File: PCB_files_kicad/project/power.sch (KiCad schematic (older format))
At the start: 21 parts, among them J7 Barrel_Jack, J8 USB_B_Micro, Q1 IRF7240PBF, U2 TP4056, U3 MT3608

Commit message: PCB - Placing components
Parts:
- BT1: footprint (none) -> TerminalBlock:TerminalBlock_bornier-2_P5.08mm
- C1, C2, C3, C5: footprint (none) -> Capacitor_THT:C_Disc_D5.0mm_W2.5mm_P5.00mm
- D3: footprint (none) -> Diode_THT:D_DO-15_P12.70mm_Horizontal
- D4: footprint (none) -> LED_THT:LED_D5.0mm; Mouser Link https://ar.mouser.com/ProductDetail/Wurth-Elektronik/150060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 -> (none); Mouser Number 710-150060VS75000 -> (none); Part Number 150060VS75000 -> (none)
- D5: value CDBU0130L - 350mV -> SS34; footprint (none) -> Diode_THT:D_DO-15_P12.70mm_Horizontal; Mouser Link https://ar.mouser.com/ProductDetail/Comchip-Technology/CDBU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 -> (none); Mouser Number 750-CDBU0130L -> (none); Part Number CDBU0130L -> (none)
- J7: footprint (none) -> Connector_BarrelJack:BarrelJack_Horizontal
- J8: footprint (none) -> Connector_USB:USB_Micro-B_Amphenol_10104110_Horizontal
- L1: footprint (none) -> Inductor_THT:L_Radial_D6.0mm_P4.00mm
- R10: value 15k -> 16k-THT; footprint (none) -> Resistor_THT:R_Axial_DIN0414_L11.9mm_D4.5mm_P20.32mm_Horizontal; Mouser Link https://ar.mouser.com/ProductDetail/Bourns/CR0603-FX-1403EL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 -> (none); Mouser Number 652-CR0603FX-1403ELF -> (none); Part Number CR0603-FX-1403ELF -> (none)
- R11: value 2k -> 2k2; footprint (none) -> Resistor_THT:R_Axial_DIN0414_L11.9mm_D4.5mm_P20.32mm_Horizontal; Mouser Link https://ar.mouser.com/ProductDetail/Bourns/CR0603-FX-1403EL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 -> (none); Mouser Number 652-CR0603FX-1403ELF -> (none); Part Number CR0603-FX-1403ELF -> (none)
- R3, R4: footprint (none) -> Resistor_THT:R_Axial_DIN0414_L11.9mm_D4.5mm_P20.32mm_Horizontal
- R7: footprint (none) -> Resistor_THT:R_Axial_DIN0414_L11.9mm_D4.5mm_P20.32mm_Horizontal; Mouser Link https://ar.mouser.com/ProductDetail/Bourns/CR0603-FX-1403EL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 -> (none); Mouser Number 652-CR0603FX-1403ELF -> (none); Part Number CR0603-FX-1403ELF -> (none)
- U2: footprint (none) -> Package_TO_SOT_SMD:SC-70-8_Handsoldering
- U3: footprint Package_TO_SOT_SMD:SOT-23-6 -> Package_TO_SOT_SMD:SOT-23-6_Handsoldering

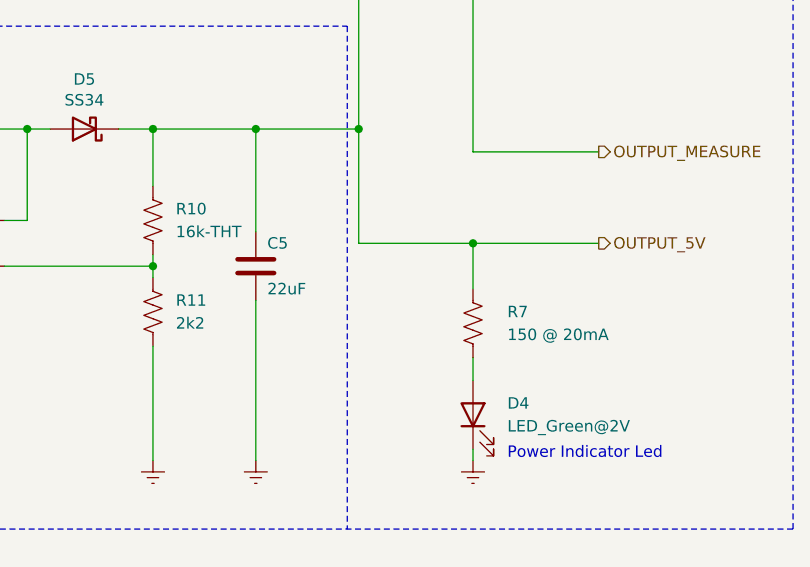
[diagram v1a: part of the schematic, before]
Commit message: PCB - Starting to route
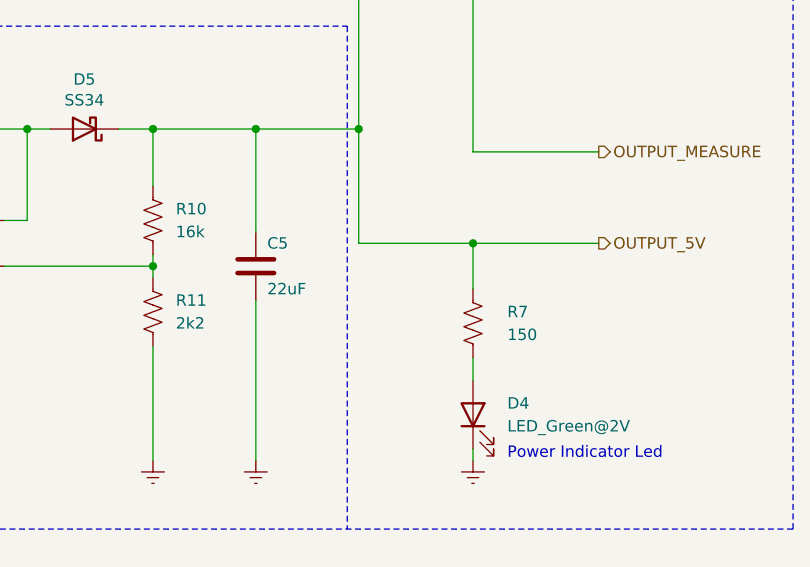
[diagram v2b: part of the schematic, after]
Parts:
- BT1: footprint TerminalBlock:TerminalBlock_bornier-2_P5.08mm -> mylib:Batt
- R10: value 16k-THT -> 16k
- R7: value 150 @ 20mA -> 150
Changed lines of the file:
@@
 F 0 "BT1" H 4350 3800 50  0000 L CNN
 F 1 "Batt" H 4350 3600 50  0000 L CNN
-F 2 "TerminalBlock:TerminalBlock_bornier-2_P5.08mm" V 4550 3710 50  0001 C CNN
+F 2 "mylib:Batt" V 4550 3710 50  0001 C CNN
 F 3 "http://www.batteryspace.com/prod-specs/4869.pdf" V 4550 3710 50  0001 C CNN
 F 4 "https://articulo.mercadolibre.com.ar/MLA-903149783-celda-18650-lg-2200mah-con-terminal-para-soldar-37v-42v-_JM?matt_tool=88481412&matt_word=&matt_source=google&matt_campaign_id=11618987428&matt_ad_group_id=113657532672&matt_match_type=&matt_network=g&matt_device=m&matt_creative=479785004862&matt_keyword=&matt_ad_position=&matt_ad_type=pla&matt_merchant_id=334313049&matt_product_id=MLA903149783&matt_product_partition_id=758317414930&matt_target_id=aud-415044759576:pla-758317414930&gclid=EAIaIQobChMI6N6ysO338QIVsyCtBh2hBgntEAQYASABEgKf_vD_BwE" H 4550 3650 50  0001 C CNN "Mouser Link"
@@
 AR Path="/60FFCFF1/6124D4A7" Ref="R7"  Part="1"
 F 0 "R7" H 9550 4100 50  0000 L CNN
-F 1 "150 @ 20mA" H 9550 4000 50  0000 L CNN
+F 1 "150" H 9550 4000 50  0000 L CNN
 F 2 "Resistor_THT:R_Axial_DIN0414_L11.9mm_D4.5mm_P20.32mm_Horizontal" V 9440 4040 50  0001 C CNN
 F 3 "" H 9400 4050 50  0001 C CNN
@@
 AR Path="/60FFCFF1/61443227" Ref="R10"  Part="1"
 F 0 "R10" H 8100 3650 50  0000 L CNN
-F 1 "16k-THT" H 8100 3550 50  0000 L CNN
+F 1 "16k" H 8100 3550 50  0000 L CNN
 F 2 "Resistor_THT:R_Axial_DIN0414_L11.9mm_D4.5mm_P20.32mm_Horizontal" V 8040 3590 50  0001 C CNN
 F 3 "" H 8000 3600 50  0001 C CNN

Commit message: SCH version 1.3
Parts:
- added TP1: PowerSupply, TestPoint:TestPoint_THTPad_D2.0mm_Drill1.0mm, symbol Connector:TestPoint
- added TP2: Batt, TestPoint:TestPoint_THTPad_D2.0mm_Drill1.0mm, symbol Connector:TestPoint
- added TP3: Qdrain, TestPoint:TestPoint_THTPad_D2.0mm_Drill1.0mm, symbol Connector:TestPoint
- added TP4: out5v, TestPoint:TestPoint_THTPad_D2.0mm_Drill1.0mm, symbol Connector:TestPoint
- Q1: value IRF7240PBF -> Irf9z20; footprint Package_TO_SOT_SMD:TO-252-2 -> Package_TO_SOT_THT:TO-220-3_Vertical
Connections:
- net OUTPUT_5V: now also TP4.1
- net OUTPUT_BAT: now also TP2.1
- net OUTPUT_MEASURE: now also TP1.1
- net at C3.1, L1.1, Q1.2 (D)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: now also TP3.1
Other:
- note added: "|VGS(ON)| > |-3.7v|"
- note removed: "-4.5v > VGS"
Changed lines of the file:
@@
 Sheet 2 3
 Title "Sistema de Alarma"
-Date "2021-07-23"
-Rev "v1.2"
+Date "2021-09-15"
+Rev "v1.3"
 Comp "Proyecto Técnicas Digitales II - Grupo N°4"
 Comment1 "Liaño, Lucas"
@@
 P 5650 3100
 F 0 "Q1" V 5550 2950 50  0000 C CNN
-F 1 "IRF7240PBF" V 5600 3450 50  0000 C CNN
-F 2 "Package_TO_SOT_SMD:TO-252-2" H 5850 3200 50  0001 C CNN
-F 3 "https://pdf1.alldatasheet.es/datasheet-pdf/view/68328/IRF/IRF9540N.html" H 5650 3100 50  0001 C CNN
+F 1 "Irf9z20" V 5550 3300 50  0000 C CNN
+F 2 "Package_TO_SOT_THT:TO-220-3_Vertical" H 5850 3200 50  0001 C CNN
+F 3 "https://www.vishay.com/docs/90121/sihf9z20.pdf" H 5650 3100 50  0001 C CNN
 F 4 "" H 5650 3100 50  0001 C CNN "Mouser Link"
 F 5 "ver en electrocomponentes!" H 5650 3100 50  0001 C CNN "Mouser Number"
@@
 	1    0    0    -1
 $EndComp
-Text Notes 5350 3500 0    50   ~ 0
--4.5v > VGS
+Text Notes 5400 3500 0    30   ~ 0
+|VGS(ON)| > |-3.7v|
 $Comp
 L Device:R_US R?
@@
 EndData
 $EndBitmap
+$Comp
+L Connector:TestPoint TP1
+U 1 1 6136A15D
+P 3450 2450
+F 0 "TP1" H 3508 2568 50  0000 L CNN
+F 1 "PowerSupply" H 3500 2650 50  0000 L CNN
+F 2 "TestPoint:TestPoint_THTPad_D2.0mm_Drill1.0mm" H 3650 2450 50  0001 C CNN
+F 3 "~" H 3650 2450 50  0001 C CNN
+	1    3450 2450
+	1    0    0    -1
+$EndComp
+$Comp
+L Connector:TestPoint TP2
+U 1 1 6136C229
+P 5100 3200
+F 0 "TP2" H 5158 3318 50  0000 L CNN
+F 1 "Batt" H 5150 3250 50  0000 L CNN
+F 2 "TestPoint:TestPoint_THTPad_D2.0mm_Drill1.0mm" H 5300 3200 50  0001 C CNN
+F 3 "~" H 5300 3200 50  0001 C CNN
+	1    5100 3200
+	1    0    0    -1
+$EndComp
+$Comp
+L Connector:TestPoint TP3
+U 1 1 613711A3
+P 6050 3200
+F 0 "TP3" H 6108 3318 50  0000 L CNN
+F 1 "Qdrain" H 6100 3250 50  0000 L CNN
+F 2 "TestPoint:TestPoint_THTPad_D2.0mm_Drill1.0mm" H 6250 3200 50  0001 C CNN
+F 3 "~" H 6250 3200 50  0001 C CNN
+	1    6050 3200
+	1    0    0    -1
+$EndComp
+$Comp
+L Connector:TestPoint TP4
+U 1 1 61377A4F
+P 9400 3700
+F 0 "TP4" H 9458 3818 50  0000 L CNN
+F 1 "out5v" H 9450 3750 50  0000 L CNN
+F 2 "TestPoint:TestPoint_THTPad_D2.0mm_Drill1.0mm" H 9600 3700 50  0001 C CNN
+F 3 "~" H 9600 3700 50  0001 C CNN
+	1    9400 3700
+	1    0    0    -1
+$EndComp
 $EndSCHEMATC

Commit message: Lot of changes.. BOM was added and UTN logo too
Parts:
- C3: value 22uF-X5R -> 22uF
- Q1: value Irf9z20 -> IRF9Z20
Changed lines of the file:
@@
 P 5650 3100
 F 0 "Q1" V 5550 2950 50  0000 C CNN
-F 1 "Irf9z20" V 5550 3300 50  0000 C CNN
+F 1 "IRF9Z20" V 5550 3300 50  0000 C CNN
 F 2 "Package_TO_SOT_THT:TO-220-3_Vertical" H 5850 3200 50  0001 C CNN
 F 3 "https://www.vishay.com/docs/90121/sihf9z20.pdf" H 5650 3100 50  0001 C CNN
@@
 AR Path="/60FFCFF1/61045CAF" Ref="C3"  Part="1"
 F 0 "C3" H 6100 4000 50  0000 L CNN
-F 1 "22uF-X5R" H 6100 3800 50  0000 L CNN
+F 1 "22uF" H 6100 3800 50  0000 L CNN
 F 2 "Capacitor_THT:C_Disc_D5.0mm_W2.5mm_P5.00mm" H 6088 3750 50  0001 C CNN
 F 3 "~" H 6050 3900 50  0001 C CNN
@@
 Text HLabel 9950 3700 2    50   Output ~ 0
 OUTPUT_5V
-Text Notes 1200 7650 0    50   ~ 10
-Circuit reference: https://www.youtube.com/watch?v=GRd9uTwg7r4
 Wire Wire Line
 	4850 2450 4850 2100
@@
 	1    0    0    -1
 $EndComp
+Text Notes 1200 7650 0    50   ~ 10
+Circuit reference: https://www.youtube.com/watch?v=GRd9uTwg7r4
 $EndSCHEMATC

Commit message: Sche rev 1.4 - PCB rev 1.2
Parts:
- C1, C2, C3, C5: footprint Capacitor_THT:C_Disc_D5.0mm_W2.5mm_P5.00mm -> Capacitor_THT:CP_Radial_D5.0mm_P2.50mm
- R10, R11, R3, R4, R7: footprint Resistor_THT:R_Axial_DIN0414_L11.9mm_D4.5mm_P20.32mm_Horizontal -> Resistor_THT:R_Axial_DIN0309_L9.0mm_D3.2mm_P12.70mm_Horizontal
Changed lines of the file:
@@
 Sheet 2 3
 Title "Sistema de Alarma"
-Date "2021-09-15"
-Rev "v1.3"
+Date "2021-09-23"
+Rev "v1.4"
 Comp "Proyecto Técnicas Digitales II - Grupo N°4"
 Comment1 "Liaño, Lucas"
@@
 F 0 "C1" H 2450 3850 50  0000 L CNN
 F 1 "10uF" H 2400 3650 50  0000 L CNN
-F 2 "Capacitor_THT:C_Disc_D5.0mm_W2.5mm_P5.00mm" H 2638 3600 50  0001 C CNN
+F 2 "Capacitor_THT:CP_Radial_D5.0mm_P2.50mm" H 2638 3600 50  0001 C CNN
 F 3 "~" H 2600 3750 50  0001 C CNN
 	1    2600 3750
@@
 F 0 "R4" H 4918 2796 50  0000 L CNN
 F 1 "10k" H 4918 2705 50  0000 L CNN
-F 2 "Resistor_THT:R_Axial_DIN0414_L11.9mm_D4.5mm_P20.32mm_Horizontal" V 4890 2740 50  0001 C CNN
+F 2 "Resistor_THT:R_Axial_DIN0309_L9.0mm_D3.2mm_P12.70mm_Horizontal" V 4890 2740 50  0001 C CNN
 F 3 "~" H 4850 2750 50  0001 C CNN
 	1    4850 2750
@@
 F 0 "C5" H 8500 3900 50  0000 L CNN
 F 1 "22uF" H 8500 3700 50  0000 L CNN
-F 2 "Capacitor_THT:C_Disc_D5.0mm_W2.5mm_P5.00mm" H 8488 3650 50  0001 C CNN
+F 2 "Capacitor_THT:CP_Radial_D5.0mm_P2.50mm" H 8488 3650 50  0001 C CNN
 F 3 "~" H 8450 3800 50  0001 C CNN
 	1    8450 3800
@@
 F 0 "C3" H 6100 4000 50  0000 L CNN
 F 1 "22uF" H 6100 3800 50  0000 L CNN
-F 2 "Capacitor_THT:C_Disc_D5.0mm_W2.5mm_P5.00mm" H 6088 3750 50  0001 C CNN
+F 2 "Capacitor_THT:CP_Radial_D5.0mm_P2.50mm" H 6088 3750 50  0001 C CNN
 F 3 "~" H 6050 3900 50  0001 C CNN
 	1    6050 3900
@@
 F 0 "R3" H 4218 4146 50  0000 L CNN
 F 1 "2.4k" H 4218 4055 50  0000 L CNN
-F 2 "Resistor_THT:R_Axial_DIN0414_L11.9mm_D4.5mm_P20.32mm_Horizontal" V 4190 4090 50  0001 C CNN
+F 2 "Resistor_THT:R_Axial_DIN0309_L9.0mm_D3.2mm_P12.70mm_Horizontal" V 4190 4090 50  0001 C CNN
 F 3 "~" H 4150 4100 50  0001 C CNN
 	1    4150 4100
@@
 F 0 "R7" H 9550 4100 50  0000 L CNN
 F 1 "150" H 9550 4000 50  0000 L CNN
-F 2 "Resistor_THT:R_Axial_DIN0414_L11.9mm_D4.5mm_P20.32mm_Horizontal" V 9440 4040 50  0001 C CNN
+F 2 "Resistor_THT:R_Axial_DIN0309_L9.0mm_D3.2mm_P12.70mm_Horizontal" V 9440 4040 50  0001 C CNN
 F 3 "" H 9400 4050 50  0001 C CNN
 F 4 "" H 9400 4050 50  0001 C CNN "Mouser Link"
@@
 F 0 "C2" H 4950 3700 50  0000 L CNN
 F 1 "10uF" H 4900 3450 50  0000 L CNN
-F 2 "Capacitor_THT:C_Disc_D5.0mm_W2.5mm_P5.00mm" H 5138 3450 50  0001 C CNN
+F 2 "Capacitor_THT:CP_Radial_D5.0mm_P2.50mm" H 5138 3450 50  0001 C CNN
 F 3 "~" H 5100 3600 50  0001 C CNN
 	1    5100 3600
@@
 F 0 "R10" H 8100 3650 50  0000 L CNN
 F 1 "16k" H 8100 3550 50  0000 L CNN
-F 2 "Resistor_THT:R_Axial_DIN0414_L11.9mm_D4.5mm_P20.32mm_Horizontal" V 8040 3590 50  0001 C CNN
+F 2 "Resistor_THT:R_Axial_DIN0309_L9.0mm_D3.2mm_P12.70mm_Horizontal" V 8040 3590 50  0001 C CNN
 F 3 "" H 8000 3600 50  0001 C CNN
 F 4 "" H 8000 3600 50  0001 C CNN "Mouser Link"
@@
 F 0 "R11" H 8100 4050 50  0000 L CNN
 F 1 "2k2" H 8100 3950 50  0000 L CNN
-F 2 "Resistor_THT:R_Axial_DIN0414_L11.9mm_D4.5mm_P20.32mm_Horizontal" V 8040 3990 50  0001 C CNN
+F 2 "Resistor_THT:R_Axial_DIN0309_L9.0mm_D3.2mm_P12.70mm_Horizontal" V 8040 3990 50  0001 C CNN
 F 3 "" H 8000 4000 50  0001 C CNN
 F 4 "" H 8000 4000 50  0001 C CNN "Mouser Link"

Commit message: Schematic v1.5 - PCB v1.3
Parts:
- D3: value CDBU0130L - 350mV -> 1N5822 - 500mV; footprint Diode_THT:D_DO-15_P12.70mm_Horizontal -> Diode_THT:D_DO-201AD_P15.24mm_Horizontal; Mouser Link https://ar.mouser.com/ProductDetail/Comchip-Technology/CDBU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 -> (none); Mouser Number 750-CDBU0130L -> (none); Part Number CDBU0130L -> (none)
- D5: value SS34 -> 1N5822 - 500mV; footprint Diode_THT:D_DO-15_P12.70mm_Horizontal -> Diode_THT:D_DO-201AD_P15.24mm_Horizontal
- R10: value 16k -> 15k
- R3: value 2.4k -> 2k2
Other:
- note added: "Battery Charge Module @ 545mA\n\n"
- note removed: "Battery Charge Module @ 500mA\n\n"
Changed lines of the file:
@@
 Sheet 2 3
 Title "Sistema de Alarma"
-Date "2021-09-23"
-Rev "v1.4"
+Date "2021-09-26"
+Rev "v1.5"
 Comp "Proyecto Técnicas Digitales II - Grupo N°4"
 Comment1 "Liaño, Lucas"
@@
 P 6150 2450
 F 0 "D3" H 6150 2233 50  0000 C CNN
-F 1 "CDBU0130L - 350mV" H 6150 2324 50  0000 C CNN
-F 2 "Diode_THT:D_DO-15_P12.70mm_Horizontal" H 6150 2450 50  0001 C CNN
-F 3 "https://ar.mouser.com/datasheet/2/80/CDBU0130L_HF_RevA748574-2490037.pdf" H 6150 2450 50  0001 C CNN
-F 4 "https://ar.mouser.com/ProductDetail/Comchip-Technology/CDBU0130L?qs=tw%252BuQ%2FB6PO2Mup5%252Bk7mubQ%3D%3D" H 6150 2450 50  0001 C CNN "Mouser Link"
-F 5 "750-CDBU0130L " H 6150 2450 50  0001 C CNN "Mouser Number"
-F 6 "CDBU0130L " H 6150 2450 50  0001 C CNN "Part Number"
+F 1 "1N5822 - 500mV" H 6150 2324 50  0000 C CNN
+F 2 "Diode_THT:D_DO-201AD_P15.24mm_Horizontal" H 6150 2450 50  0001 C CNN
+F 3 "https://www.vishay.com/docs/88526/1n5820.pdf" H 6150 2450 50  0001 C CNN
+F 4 "" H 6150 2450 50  0001 C CNN "Mouser Link"
+F 5 "" H 6150 2450 50  0001 C CNN "Mouser Number"
+F 6 "" H 6150 2450 50  0001 C CNN "Part Number"
 	1    6150 2450
 	-1   0    0    1
@@
 AR Path="/60FFCFF1/61001D30" Ref="R3"  Part="1"
 F 0 "R3" H 4218 4146 50  0000 L CNN
-F 1 "2.4k" H 4218 4055 50  0000 L CNN
+F 1 "2k2" H 4218 4055 50  0000 L CNN
 F 2 "Resistor_THT:R_Axial_DIN0309_L9.0mm_D3.2mm_P12.70mm_Horizontal" V 4190 4090 50  0001 C CNN
 F 3 "~" H 4150 4100 50  0001 C CNN
@@
 $EndComp
 Text Notes 2800 5000 0    50   ~ 0
-Battery Charge Module @ 500mA\n\n
+Battery Charge Module @ 545mA\n\n
 $Comp
 L Device:LED D4
@@
 P 7700 3200
 F 0 "D5" H 7700 2983 50  0000 C CNN
-F 1 "SS34" H 7700 3074 50  0000 C CNN
-F 2 "Diode_THT:D_DO-15_P12.70mm_Horizontal" H 7700 3200 50  0001 C CNN
-F 3 "" H 7700 3200 50  0001 C CNN
+F 1 "1N5822 - 500mV" H 7700 3074 50  0000 C CNN
+F 2 "Diode_THT:D_DO-201AD_P15.24mm_Horizontal" H 7700 3200 50  0001 C CNN
+F 3 "https://www.vishay.com/docs/88526/1n5820.pdf" H 7700 3200 50  0001 C CNN
 F 4 "" H 7700 3200 50  0001 C CNN "Mouser Link"
 F 5 "" H 7700 3200 50  0001 C CNN "Mouser Number"
@@
 AR Path="/60FFCFF1/61443227" Ref="R10"  Part="1"
 F 0 "R10" H 8100 3650 50  0000 L CNN
-F 1 "16k" H 8100 3550 50  0000 L CNN
+F 1 "15k" H 8100 3550 50  0000 L CNN
 F 2 "Resistor_THT:R_Axial_DIN0309_L9.0mm_D3.2mm_P12.70mm_Horizontal" V 8040 3590 50  0001 C CNN
 F 3 "" H 8000 3600 50  0001 C CNN

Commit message: Schematic v1.6
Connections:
- net at J8.2 (D-): no longer J8.3 (D+)
- no-connect marks 2 -> 4
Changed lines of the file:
@@
 Sheet 2 3
 Title "Sistema de Alarma"
-Date "2021-09-26"
-Rev "v1.5"
+Date "2021-09-27"
+Rev "v1.6"
 Comp "Proyecto Técnicas Digitales II - Grupo N°4"
 Comment1 "Liaño, Lucas"
@@
 $EndComp
 Wire Wire Line
-	1800 3450 1800 3350
-Wire Wire Line
 	1850 3850 1500 3850
 Wire Wire Line
@@
 Wire Wire Line
 	1800 3550 1850 3550
-$Comp
-L Connector:USB_B_Micro J?
-U 1 1 61001D56
-P 1500 3350
-AR Path="/60FAC4BE/61001D56" Ref="J?"  Part="1"
-AR Path="/60FFCFF1/61001D56" Ref="J8"  Part="1"
-F 0 "J8" H 1557 3817 50  0000 C CNN
-F 1 "USB_B_Micro" H 1557 3726 50  0000 C CNN
-F 2 "Connector_USB:USB_Micro-B_Amphenol_10104110_Horizontal" H 1650 3300 50  0001 C CNN
-F 3 "~" H 1650 3300 50  0001 C CNN
-	1    1500 3350
-	1    0    0    -1
-$EndComp
 $Comp
 L power:Earth #PWR?
@@
 Text Notes 1200 7650 0    50   ~ 10
 Circuit reference: https://www.youtube.com/watch?v=GRd9uTwg7r4
+$Comp
+L Connector:USB_B_Micro J?
+U 1 1 61001D56
+P 1500 3350
+AR Path="/60FAC4BE/61001D56" Ref="J?"  Part="1"
+AR Path="/60FFCFF1/61001D56" Ref="J8"  Part="1"
+F 0 "J8" H 1557 3817 50  0000 C CNN
+F 1 "USB_B_Micro" H 1557 3726 50  0000 C CNN
+F 2 "Connector_USB:USB_Micro-B_Amphenol_10104110_Horizontal" H 1650 3300 50  0001 C CNN
+F 3 "~" H 1650 3300 50  0001 C CNN
+	1    1500 3350
+	1    0    0    -1
+$EndComp
+NoConn ~ 1800 3450
+NoConn ~ 1800 3350
 $EndSCHEMATC

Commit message: Schematic v1.7 - PCB v1.4
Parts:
- added C2: 10uF, Capacitor_SMD:C_0805_2012Metric_Pad1.18x1.45mm_HandSolder, symbol Device:C
- added U3: LM1117-3.3, Package_TO_SOT_SMD:SOT-223-3_TabPin2, symbol Regulator_Linear:LM1117-3.3
- TP2: renamed from TP1; value PowerSupply -> Vin
- TP5: renamed from TP4; value out5v -> +5V
- renumbered C2 to C3, C3 to C4, D5 to D4, D4 to D5, R4 to R10, R10 to R11, R11 to R12, R7 to R13, R3 to R9, TP2 to TP3, TP3 to TP4, U3 to U4
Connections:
- net Earth: now also C2.2, U3.1 (GND)
- net OUTPUT_5V: now also U3.3 (VI)
- new net OUTPUT_3V3: C2.1, U3.2 (VO)
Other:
- note added: "Voltage Regulator 3.3V\n"
